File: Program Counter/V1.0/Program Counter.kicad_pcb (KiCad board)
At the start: 2 copper layers, 200 x 139 mm, 45 parts, among them J1 PC_OUT, J2 PC_OFFS, J3 Control, J4 Clock, J5 POWER/GND

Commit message: 25oct
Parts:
- J1, J2: footprint Connectors_JST:JST_XH_B16B-XH-A_16x2.50mm_Straight -> Kicad Libraries:16pinIDC

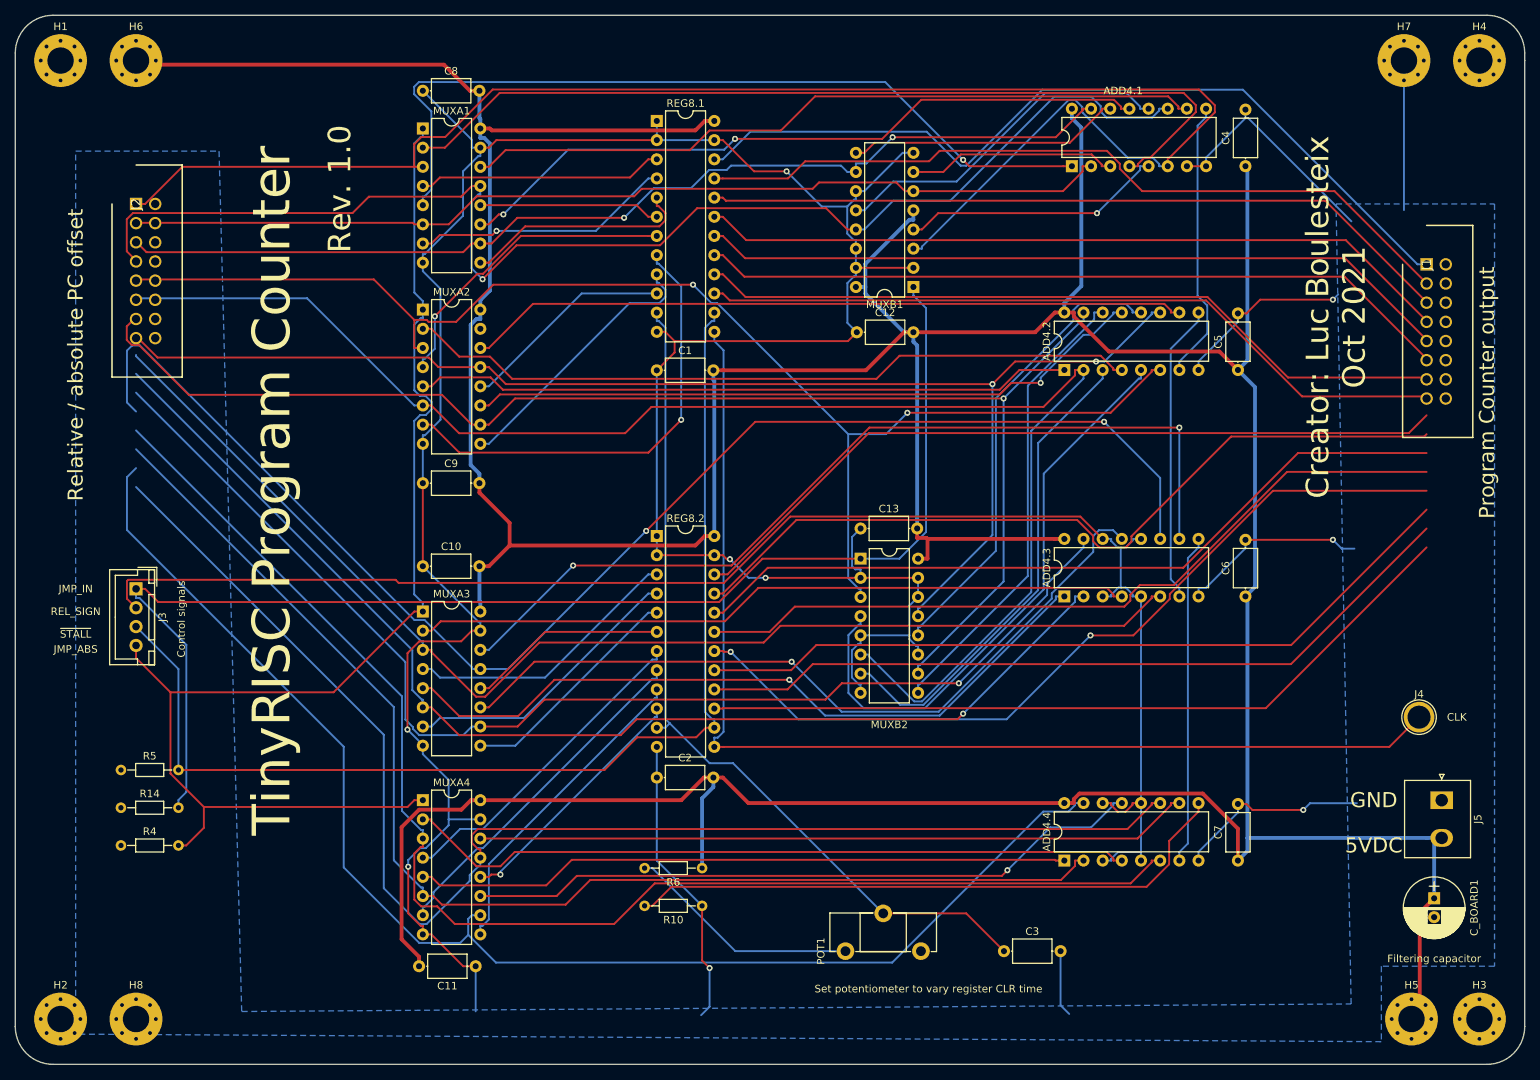
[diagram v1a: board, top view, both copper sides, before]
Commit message: 27oct
Finished v1.0 of ALU, PC and GP RF.
Updated documentation to match.
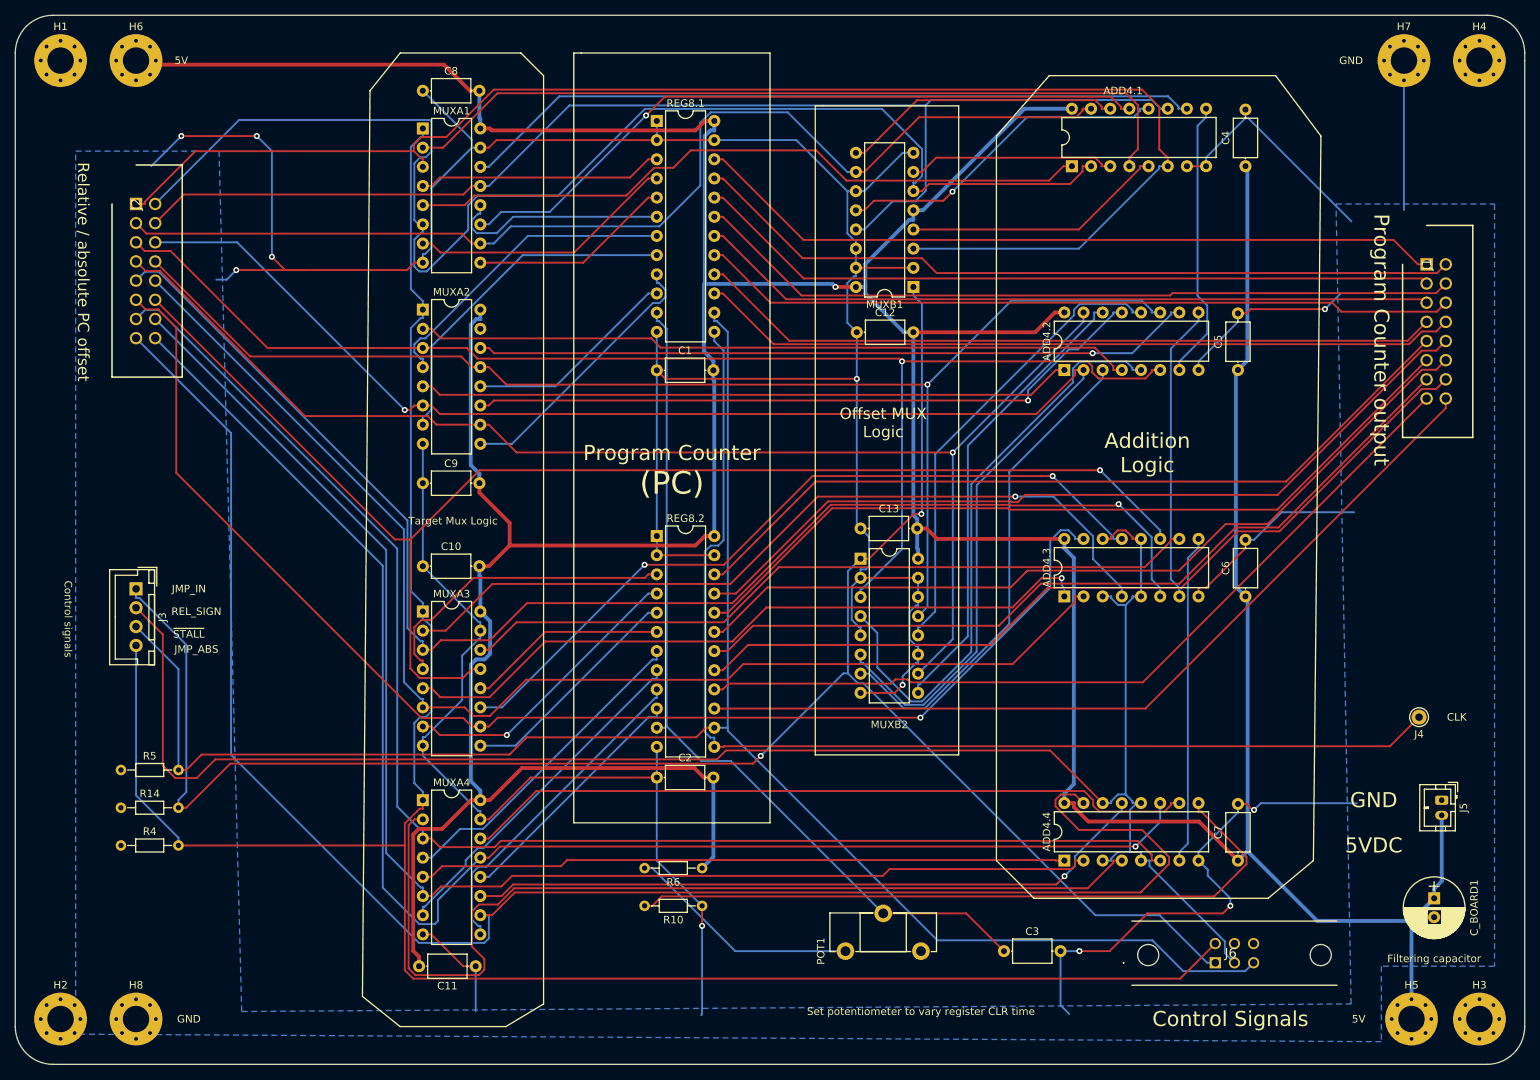
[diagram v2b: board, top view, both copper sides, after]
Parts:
- added J6: Control, Kicad libraries:6pinIDC, F.Cu at (199.0, 144.5)
- J1, J2: footprint Kicad Libraries:16pinIDC -> Kicad libraries:16pinIDC
- J4: footprint Connectors:1pin -> Connector_Pin:Pin_D1.0mm_L10.0mm
- J5: footprint Connectors_JST:JST_NV_B02P-NV_2x5.00mm_Vertical -> Connector_JST:JST_PH_B2B-PH-K_1x02_P2.00mm_Vertical
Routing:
- net JMP_ABS: track 168.4 -> 286.8 mm
- net ~STALL: track 151.1 -> 236.1 mm
- net GNDREF: track 569.1 -> 650.8 mm, vias 9 -> 11
- net JMP_IN: track 174.9 -> 250.1 mm, vias 0 -> 2
- net /OFF14: track 182.3 -> 227.5 mm
- net /OFF1: track 131.2 -> 175.6 mm
- net REL_SIGN: track 203.4 -> 236.7 mm
- net /S12: track 96.8 -> 129.4 mm
- net /OFF8: track 161.0 -> 183.0 mm, vias 0 -> 1
- net /S11: track 119.6 -> 98.9 mm, vias 2 -> 0
- net /S1: track 109.2 -> 91.5 mm, vias 1 -> 0
- net /OFF0: track 210.0 -> 192.9 mm
- net /OFF15: track 183.0 -> 200.0 mm, vias 0 -> 1
- net /OFF13: track 165.9 -> 181.2 mm
- net /N5: track 60.9 -> 45.9 mm, vias 1 -> 0
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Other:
- board text added: "(PC)"
- board text added: "5V"
- board text added: "Addition Logic"
- board text added: "Control Signals"
- board text added: "Offset MUX Logic"
- board text added: "Program Counter"
- board text added: "Target Mux Logic"
